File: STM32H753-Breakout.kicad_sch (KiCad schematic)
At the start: 0 parts

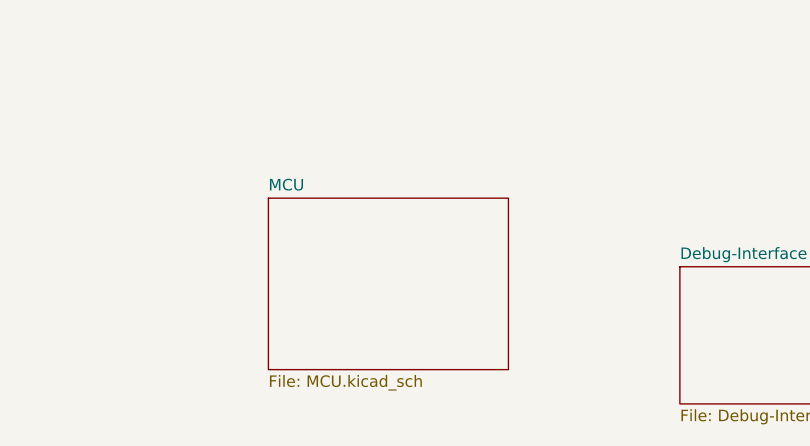
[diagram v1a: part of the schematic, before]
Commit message: added decaps to MCU, split MCU into IO and Power sheets
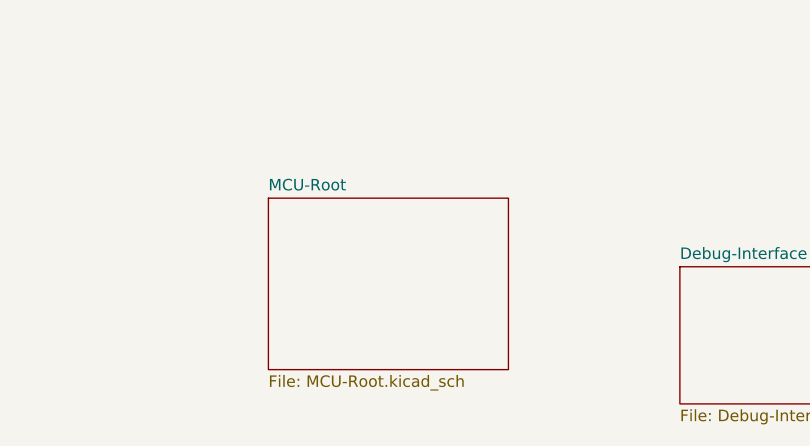
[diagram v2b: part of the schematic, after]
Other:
- sheet MCU renamed MCU-Root
- sheet MCU-Root: file MCU.kicad_sch -> MCU-Root.kicad_sch
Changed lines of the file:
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@@
 			(color 162 248 151 1.0000)
 		)
-		(property "Sheetname" "MCU"
+		(property "Sheetname" "MCU-Root"
 			(at 140.97 147.8784 0)
 			(effects
@@
 			)
 		)
-		(property "Sheetfile" "MCU.kicad_sch"
+		(property "Sheetfile" "MCU-Root.kicad_sch"
 			(at 140.97 168.2246 0)
 			(effects
